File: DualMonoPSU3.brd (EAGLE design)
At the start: 64 x 90 mm, 19 parts, among them J1 1935161

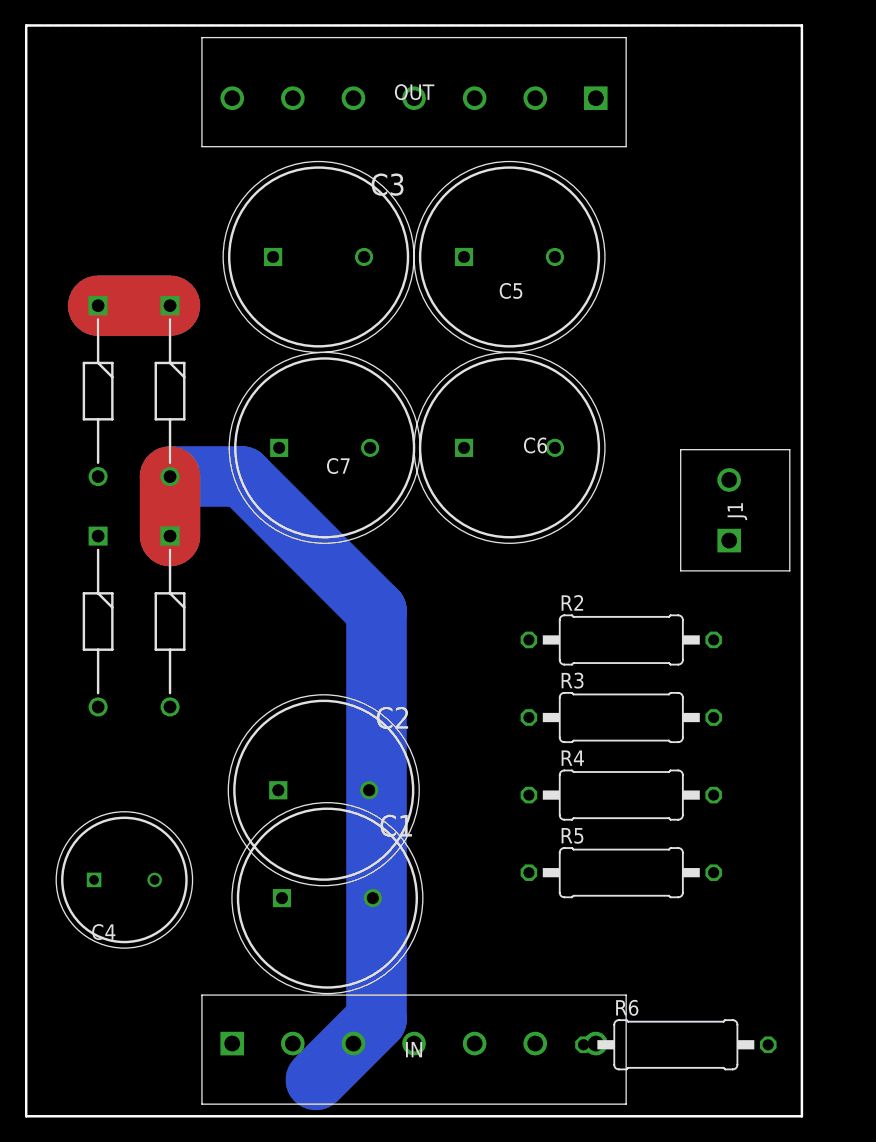
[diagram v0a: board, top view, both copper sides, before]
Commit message: submitted PSU board for fabrication
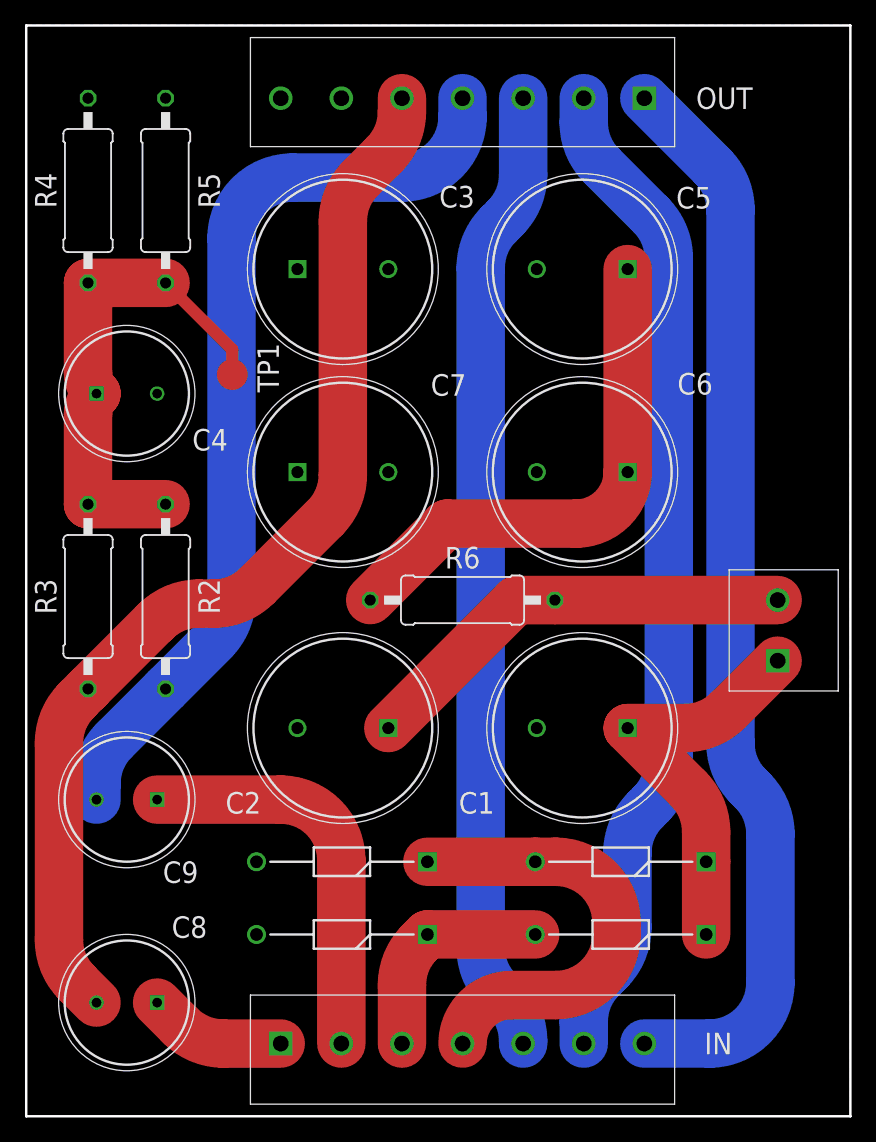
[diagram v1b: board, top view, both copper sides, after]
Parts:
- added C8, C9: UCY2E220MPD1TD, UCY2E220MPD1TD:CAPPRD500W60D1025H1750
- added TP1: TPB2,54, testpad:B2,54
- R4: value 100k -> 300k
- moved D3 68.2 mm to (56.1, 15.0), turned to 180 degrees
- moved D4 68.0 mm to (56.1, 21.0), turned to 180 degrees
- moved R5 67.7 mm to (11.5, 76.4), turned to 270 degrees
- moved R4 66.5 mm to (5.10, 76.4), turned to 90 degrees
- moved R3 45.1 mm to (5.10, 42.9), turned to 90 degrees
- moved R6 40.7 mm to (36.0, 42.6)
- moved C4 40.1 mm to (5.80, 59.6)
- moved D2 39.1 mm to (33.1, 15.0), turned to 180 degrees
- moved D1 38.2 mm to (33.1, 21.0), turned to 180 degrees
- moved R2 37.8 mm to (11.5, 42.9), turned to 270 degrees
- moved C1 31.8 mm to (49.6, 32.0), turned to 180 degrees
- moved C6 13.6 mm to (49.6, 53.1), turned to 180 degrees
- moved C5 13.5 mm to (49.6, 69.9), turned to 180 degrees
- moved J1 10.7 mm to (62.0, 37.6)
- moved C2 10.4 mm to (29.9, 32.0), turned to 180 degrees
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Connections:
- removed net N$1: IN.5, OUT.2, R3.1
- removed net N$2: D1.1, D4.2, IN.1
- removed net N$4: D2.1, D3.2, IN.2
- removed net N$7: IN.4, OUT.1, R2.2
- removed net N$8: IN.6, OUT.3
- removed net N$9: IN.7, OUT.4
- new net 115_VAC_BLK: D1.1, D4.2, IN.4
- new net 115_VAC_RED: D2.1, D3.2, IN.3
- new net 126_VAC_L: C9.2, OUT.4, R2.2
- new net 126_VAC_N: C8.2, OUT.5, R3.1
- new net 6.3_VAC_BLU: IN.7, OUT.1
- new net 6.3_VAC_BRN: C8.1, IN.1
- new net 6.3_VAC_GRN: IN.6, OUT.2
- new net 6.3_VAC_ORG: C9.1, IN.2
- net N$6: now also TP1.TP
- net PE: now also IN.5, OUT.3; no longer IN.3, OUT.5
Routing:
- net 6.3_VAC_BLU: track 0.00 -> 88.8 mm
- net 126_VAC_N: track 0.00 -> 88.6 mm
- net 6.3_VAC_GRN: track 0.00 -> 81.9 mm
- net PE: track 0.00 -> 79.6 mm
- net 126_VAC_L: track 0.00 -> 75.1 mm
- net N$4: track 67.3 -> 0.00 mm
- net VCC: track 0.00 -> 42.4 mm
- net N$6: track 0.00 -> 41.2 mm
- net N$5: track 0.00 -> 36.5 mm
- net 115_VAC_BLK: track 0.00 -> 35.1 mm
- net 6.3_VAC_ORG: track 0.00 -> 32.4 mm
- net N$3: track 5.93 -> 33.8 mm
- net 115_VAC_RED: track 0.00 -> 18.5 mm
- net 6.3_VAC_BRN: track 0.00 -> 11.3 mm
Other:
- board size 64 x 90 mm -> 68 x 90 mm

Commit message: Organization and Master BOM
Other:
- board text added: "115 VAC BLK"
- board text added: "115 VAC RED"
- board text added: "126 VAC L"
- board text added: "126 VAC N"
- board text added: "6.3 VAC BLU"
- board text added: "6.3 VAC BRN"
- board text added: "6.3 VAC GRN"
- board text added: "6.3 VAC ORG"
- board text added: "DGND"
- board text added: "PE"
- board text added: "VCC"

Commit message: Combi progress
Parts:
- renumbered C1 to C1P, C2 to C2P, C3 to C3P, C4 to C4P, C5 to C5P, C6 to C6P, C7 to C7P, C8 to C8P, C9 to C9P, R2 to R2P, R3 to R3P, R4 to R4P, R5 to R5P, R6 to R6P
